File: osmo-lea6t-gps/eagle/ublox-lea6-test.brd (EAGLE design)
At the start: 49.5 x 49.5 mm, 52 parts, among them U1 UBLOX-LEA-6T, U2 TPS73633, U3 TPS73633, X1 SERIAL, X2 ANT, X3 FOUT, X4 ANT, X5 FOUT, X6 1PPS, X7 PC, X8 1PPS, X9 22-23-2021

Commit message: Specify LED series resistor as 100 Ohms
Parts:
- R13: value (none) -> 100R
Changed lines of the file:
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@@
 </element>
 <element name="LED1" library="led" package="SML0603" value="" x="27.305" y="16.1925"/>
-<element name="R13" library="we_passive" package="0603" value="" x="24.13" y="16.1925"/>
+<element name="R13" library="we_passive" package="0603" value="100R" x="24.13" y="16.1925"/>
 <element name="TP8" library="we_conn" package="TP_1X1" value="TESTPAD" x="8.255" y="34.925" smashed="yes">
 <attribute name="NAME" x="3.8975" y="37.445" size="1.27" layer="25"/>

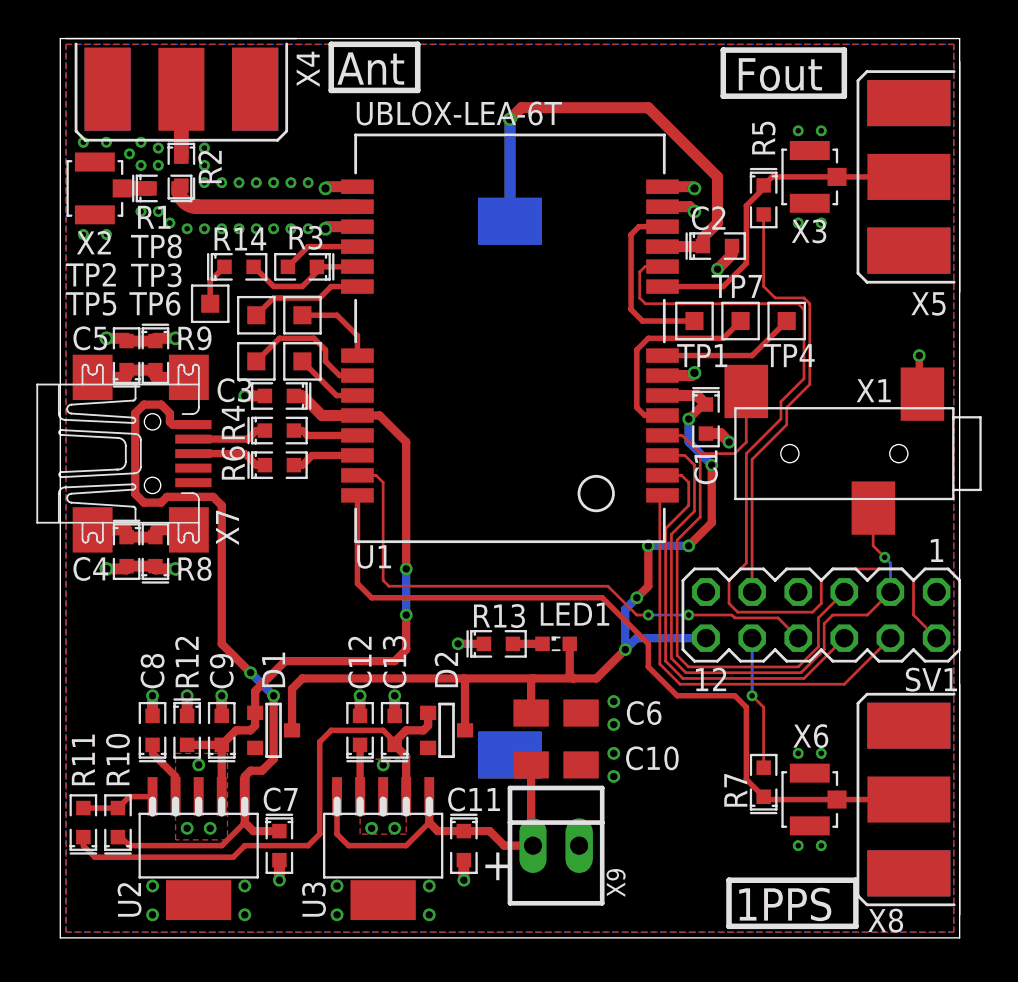
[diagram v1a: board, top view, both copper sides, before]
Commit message: add fiducials for automatic mounting of components
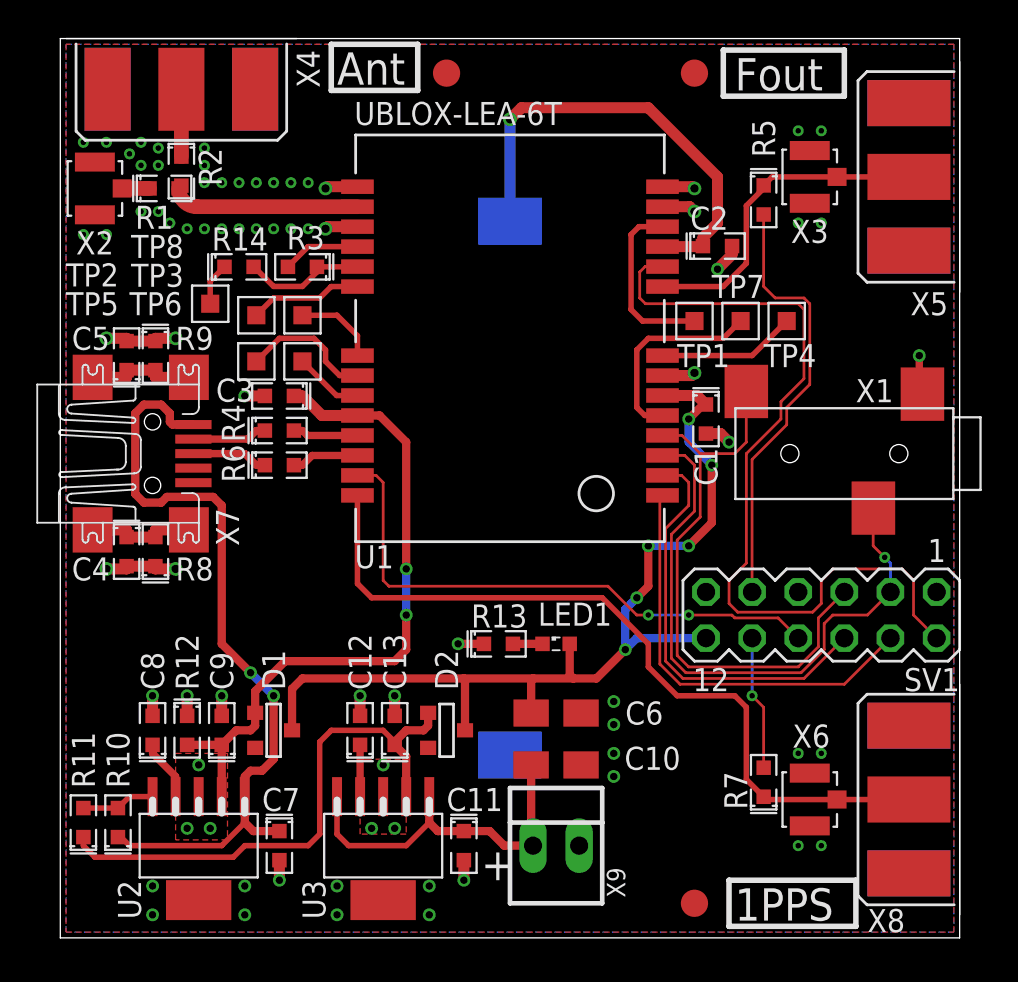
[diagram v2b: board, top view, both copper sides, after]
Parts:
- added U$30, U$31, U$32: (no value), dicons:VISION_REF15
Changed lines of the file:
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@@
 </element>
 <element name="R14" library="we_passive" package="0603" value="DNP" x="9.8425" y="36.957"/>
+<element name="U$30" library="dicons" package="VISION_REF15" value="" x="21.2725" y="47.625"/>
+<element name="U$31" library="dicons" package="VISION_REF15" value="" x="34.925" y="1.905"/>
+<element name="U$32" library="dicons" package="VISION_REF15" value="" x="34.925" y="47.625"/>
 </elements>
 <signals>
